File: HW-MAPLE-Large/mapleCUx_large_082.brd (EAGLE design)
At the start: 100 x 59 mm, 54 parts, among them IC1 DS2482-100S, IC2 LAN-USR-ES1, Q1 BSS84, X4 1751248, X7 1751264

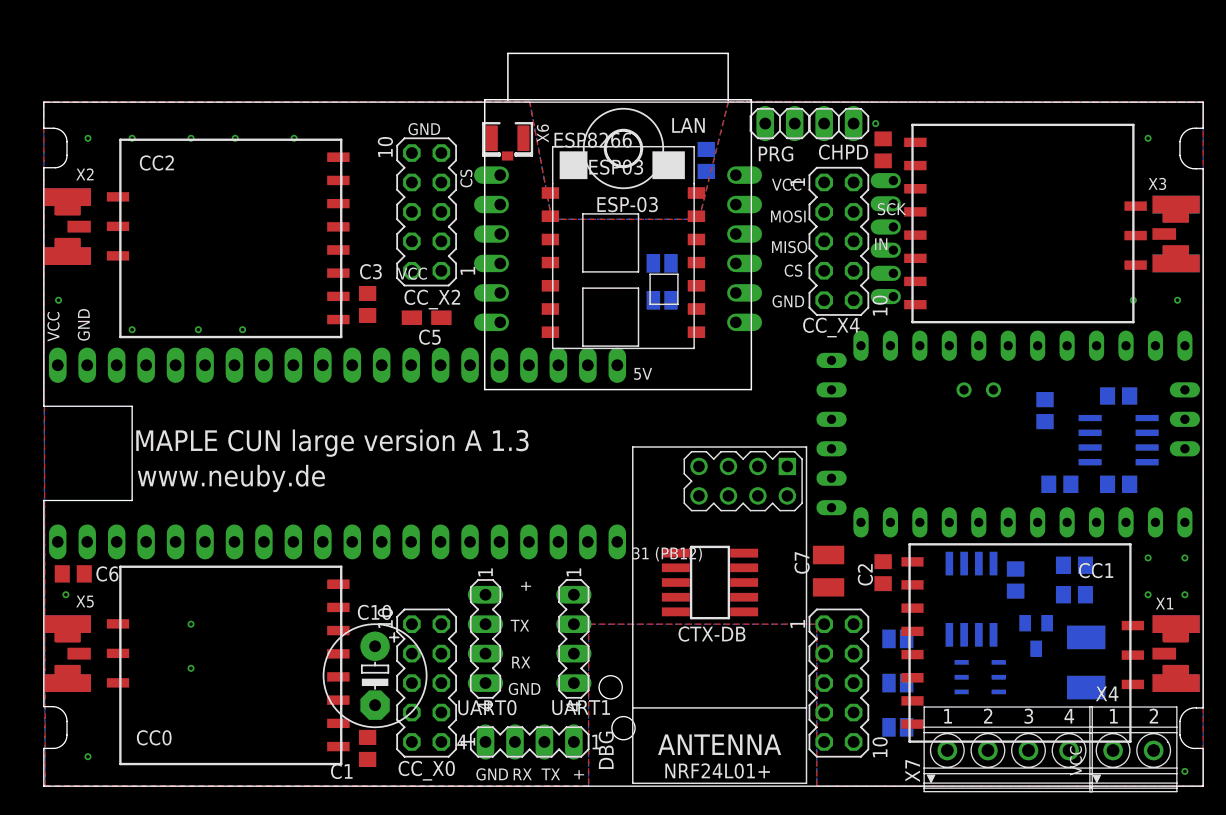
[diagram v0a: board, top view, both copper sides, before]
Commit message: Large 082 Maple moved to Top...
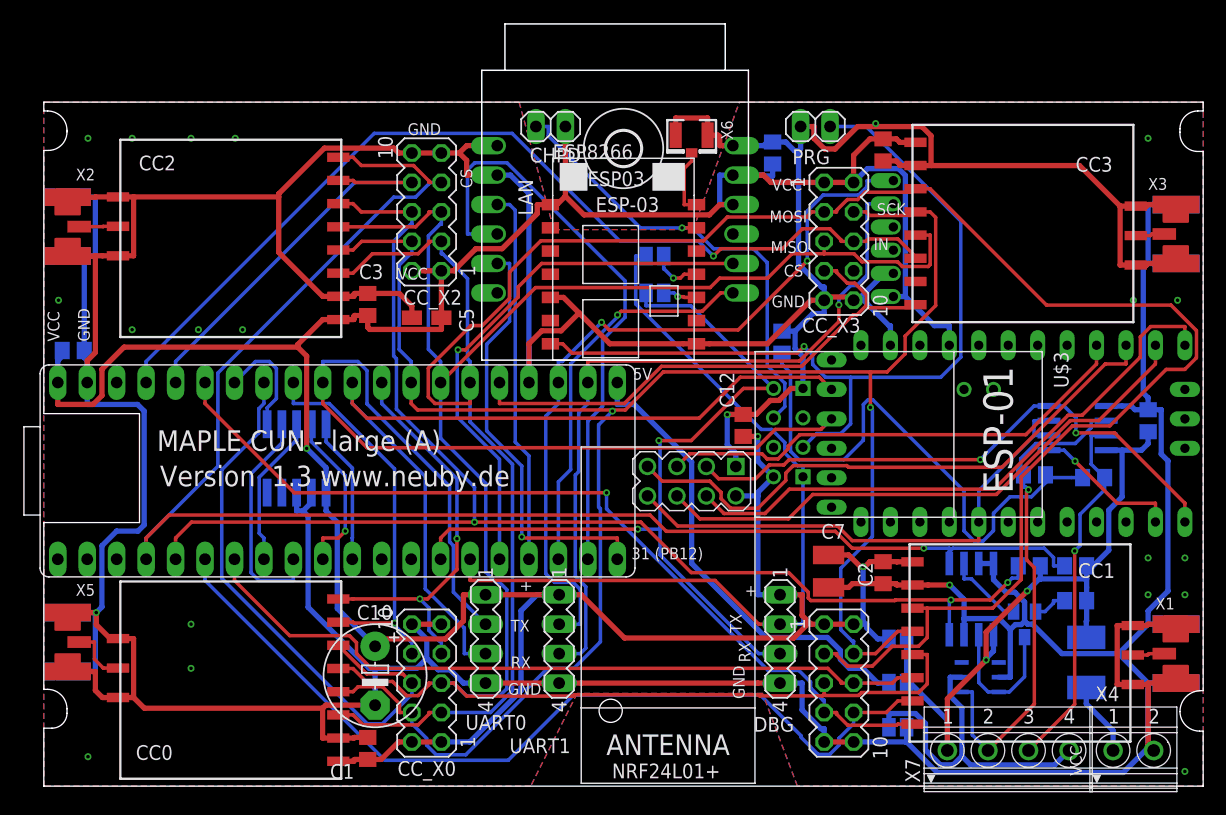
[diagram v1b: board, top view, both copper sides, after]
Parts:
- added C12: 22pF, rcl:C0805
- added U$3: ESP01, esp8266modules:ESP01
- IC1: value DS2482-100S -> DS2482
- moved CTX-DB 37.2 mm to (21.8, 28.3), flipped to the bottom, turned to 0 degrees
- moved CHPD 24.9 mm to (43.7, 56.9)
- moved C8 23.4 mm to (63.7, 38.3)
- moved DBG 23.3 mm to (63.5, 12.7), turned to 270 degrees
- moved C6 19.3 mm to (2.54, 37.6), flipped to the bottom, turned to 180 degrees
- moved X6 15.9 mm to (55.9, 56.1)
- moved C11 5.75 mm to (62.9, 54.6)
- moved NRF24L01+ 4.44 mm to (53.3, 14.9)
- moved RS485 3.69 mm to (89.2, 30.9)
- moved C9 3.32 mm to (95.2, 31.5), turned to 270 degrees
- moved PRG 3.06 mm to (66.5, 56.9)
- moved IC2 2.55 mm to (49.3, 49.5)
- moved R5 2.33 mm to (85.5, 26.8), turned to 0 degrees
- moved R3 2.24 mm to (90.5, 26.6)
- moved R2 1.70 mm to (85.0, 19.0), turned to 0 degrees
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- renumbered CC_X4 to CC_X3
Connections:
- net GND: now also C12.2, U$3.GND
- net N$11: now also U$3.GPIO0
- net N$17: now also U$3.CH_PD
- net RX_DBG: now also U$3.TX
- net SCK2: no longer IC2.5
- net TX_DBG: now also U$3.RX
- net VCC: now also C12.1, U$3.VCC
- net WIZ_CS: now also IC2.5
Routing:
- net GND: track 0.00 -> 601.7 mm, vias 0 -> 3
- net VCC: track 0.00 -> 283.7 mm, vias 0 -> 3
- net MOSI1: track 0.00 -> 209.3 mm
- net MISO1: track 0.00 -> 170.8 mm
- net SCK1: track 0.00 -> 170.2 mm, vias 0 -> 2
- net CC_CS2: track 0.00 -> 140.2 mm, vias 0 -> 1
- net CC_IN_2: track 0.00 -> 120.1 mm, vias 0 -> 3
- net CC_IN_3: track 0.00 -> 83.1 mm, vias 0 -> 1
- net TX-MAPLE: track 0.00 -> 80.4 mm
- net CC_OUT_1: track 0.00 -> 76.7 mm
- net CC_CS1: track 0.00 -> 76.2 mm, vias 0 -> 1
- net RX-MAPLE: track 0.00 -> 74.8 mm
- net N$11: track 0.00 -> 73.6 mm, vias 0 -> 1
- net RX_DBG: track 0.00 -> 71.7 mm, vias 0 -> 2
- net TX_DBG: track 0.00 -> 71.4 mm
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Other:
- outline, holes or cut-outs redrawn
- board text added: "1Wire"
- board text added: "CC3"
- board text added: "MAPLE CUN - large (A)"
- board text added: "RS485"
- board text added: "Version 1.3 www.neuby.de"
- board text removed: "MAPLE CUN large version A 1.3"
- board text removed: "www.neuby.de"
